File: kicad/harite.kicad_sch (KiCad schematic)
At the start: 76 parts, among them J1 Cirque Connector, J2 Cirque Connector, U1 RP2040_Zero, U2 RP2040_Zero

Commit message: basic schematic
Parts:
- removed D1, D10, D11, D12, D13, D14, D15, D16, D17, D18, D19, D2, D20, D21, D22, D23, D24, D25, D26, D27, D28, D29, D3, D30, D31, D32, D33, D34, D35, D36, D37, D38, D39, D4, D40, D41, D42, D43, D44, D45, D46, D47, D48, D49, D5, D50, D6, D7, D8, D9: D, ScottoKeebs_Components:Diode_SOD-123, symbol Device:D
- removed H1, H10, H2, H3, H4, H5, H6, H7, H8, H9: Mounting_Hole, MountingHole:MountingHole_2.2mm_M2_Pad_Via, symbol ScottoKeebs:Placeholder_Mounting_Hole
- removed J1, J2: Cirque Connector, footprints:Cirque-connector, symbol Connector_Generic:Conn_01x06
- removed S10, S6, S7, S8, S9: SKRHADE010, footprints:SKRHADE, symbol SKRHADE010:SKRHADE010
- removed U1, U2: RP2040_Zero, ScottoKeebs_MCU:RP2040_Zero, symbol ScottoKeebs:MCU_RP2040_Zero
- removed USB2: HRO-TYPE-C-31-M-12, footprints:HRO-TYPE-C-31-M-12, symbol USBType-C:HRO-TYPE-C-31-M-12
- added J1: 503480-0500, 5034800500, symbol 503480-0500:503480-0500
- added U3: Raspberry_Pi_Pico, ScottoKeebs_MCU:Raspberry_Pi_Pico, symbol ScottoKeebs:MCU_Raspberry_Pi_Pico
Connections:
- net Col 1 is gone; now on net GND: S1.5 (COMMON)
- net Col 2 is gone; now on net GND: S2.5 (COMMON)
- net Col 3 is gone; now on net GND: S3.5 (COMMON)
- net Col 4 is gone; now on net GND: S4.5 (COMMON)
- net Col 5 is gone; now on net GND: S5.5 (COMMON)
- net 3V3: now also J1.1, U3.36 (3V3)
- net 5V: now also U3.40 (VBUS)
- net GND: now also J1.4, U3.3 (GND)
- net GP0: now also U3.1 (GPIO0)
- net GP1: now also U3.2 (GPIO1)
- net TW: now reaches S5.3 (C)
- net TW: now also U3.25 (GPIO19)
- net PS: now reaches S1.6 (D)
- net PS: now also U3.7 (GPIO5)
- net PN: now reaches S1.1 (A)
- net PN: now also U3.4 (GPIO2)
- net PW: now reaches S1.3 (C)
- net PW: now also U3.5 (GPIO3)
- net PE: now reaches S1.4 (B)
- net PE: now also U3.6 (GPIO4)
- net IE: now reaches S4.4 (B)
- net IE: now also U3.21 (GPIO16)
- net TC: now reaches S5.2 (CENTER)
- net TC: now also U3.29 (GPIO22)
- net RN: now reaches S2.1 (A)
- net RN: now also U3.9 (GPIO6)
- net RW: now reaches S2.3 (C)
- net RW: now also U3.10 (GPIO7)
- net RE: now reaches S2.4 (B)
- net RE: now also U3.11 (GPIO8)
- net RS: now reaches S2.6 (D)
- net RS: now also U3.12 (GPIO9)
- net TN: now reaches S5.1 (A)
- net TN: now also U3.24 (GPIO18)
- net TE: now reaches S5.4 (B)
- net TE: now also U3.26 (GPIO20)
- net TS: now reaches S5.6 (D)
- net TS: now also U3.27 (GPIO21)
- net MW: now reaches S3.3 (C)
- net MW: now also U3.15 (GPIO11)
- net MS: now reaches S3.6 (D)
- net MS: now also U3.17 (GPIO13)
- net MN: now reaches S3.1 (A)
- net MN: now also U3.14 (GPIO10)
- net ME: now reaches S3.4 (B)
- net ME: now also U3.16 (GPIO12)
- net IN: now reaches S4.1 (A)
- net IN: now also U3.19 (GPIO14)
- net IW: now reaches S4.3 (C)
- net IW: now also U3.20 (GPIO15)
- net IS: now reaches S4.6 (D)
- net IS: now also U3.22 (GPIO17)
- new net JC: J1.3, U3.34 (GPIO28_ADC2)
- new net JX: J1.5, U3.31 (GPIO26_ADC0)
- new net JY: J1.2, U3.32 (GPIO27_ADC1)
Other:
- moved on the sheet: S5, USB1

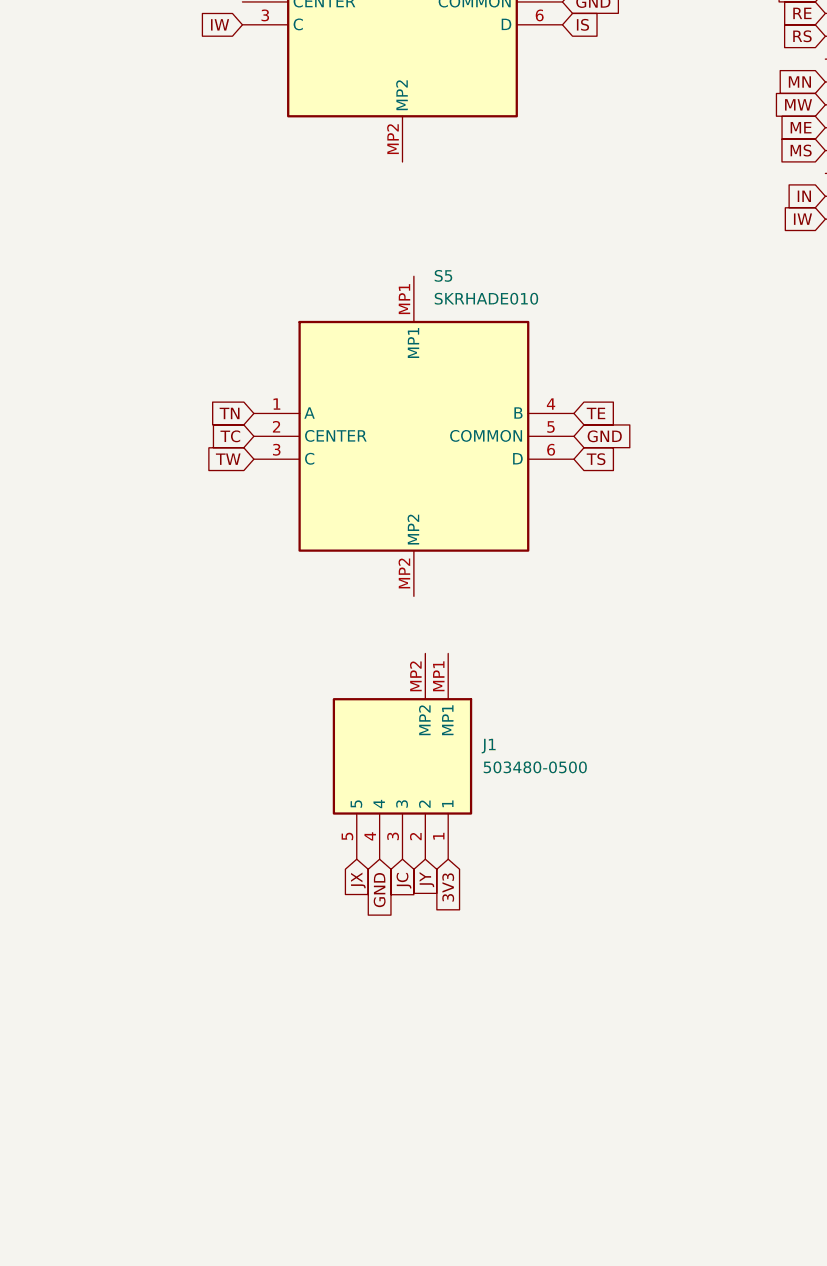
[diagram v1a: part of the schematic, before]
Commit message: Add 5034800540 and 5034801000
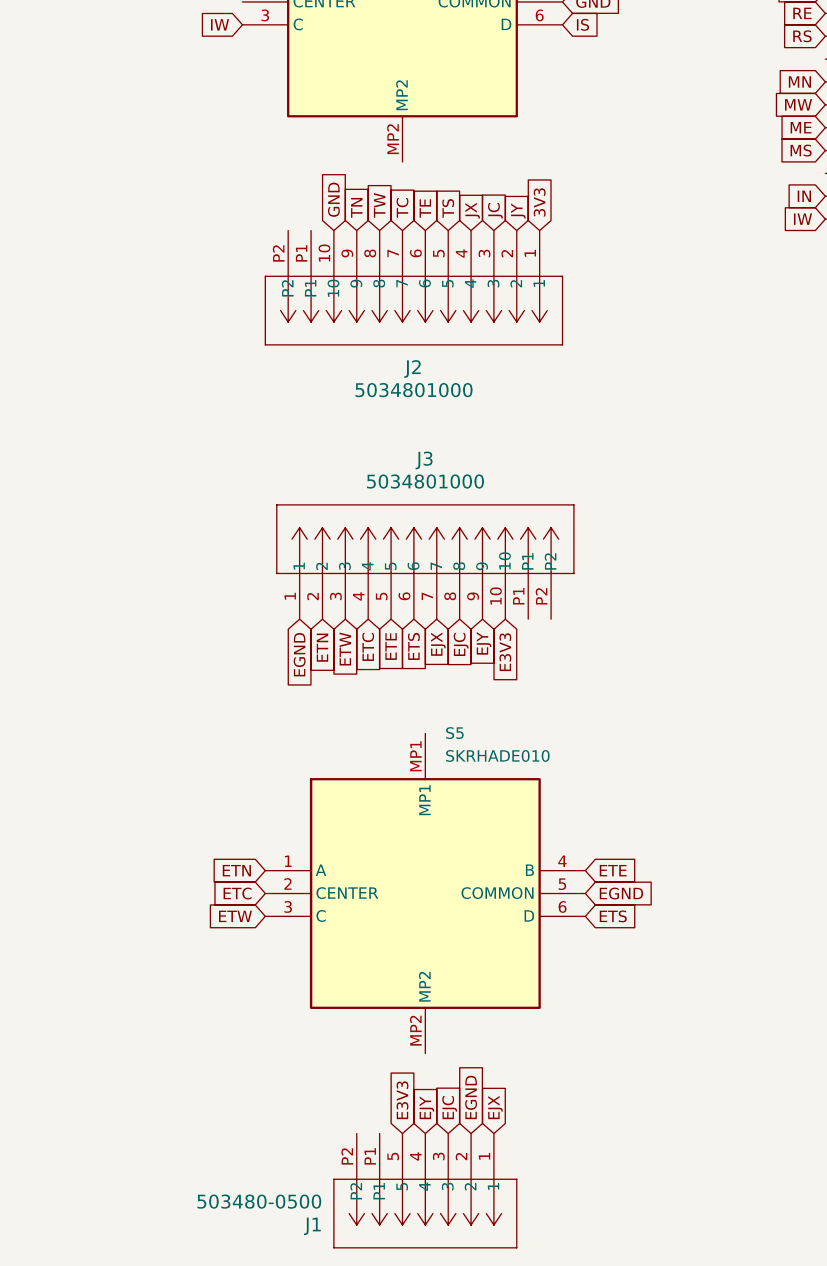
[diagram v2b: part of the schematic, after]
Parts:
- removed J1: 503480-0500, 5034800500, symbol 503480-0500:503480-0500
- added J1: 503480-0500, 5034800540, symbol 5034800540:5034800540
- added J2, J3: 5034801000, 5034801000, symbol 5034801000:5034801000
- S1, S2, S3, S4, S5: footprint footprints:SKRHADE -> SKRHADE010
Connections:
- net 3V3: now also J2.1
- net GND: now also J2.10; no longer S5.5 (COMMON)
- net JC: now also J2.3
- net JX: now also J2.4
- net JY: now also J2.2
- net TC: now also J2.7; no longer S5.2 (CENTER)
- net TE: now also J2.6; no longer S5.4 (B)
- net TN: now also J2.9; no longer S5.1 (A)
- net TS: now also J2.5; no longer S5.6 (D)
- net TW: now also J2.8; no longer S5.3 (C)
- new net E3V3: J1.5, J3.10
- new net EGND: J1.2, J3.1, S5.5 (COMMON)
- new net EJC: J1.3, J3.8
- new net EJX: J1.1, J3.7
- new net EJY: J1.4, J3.9
- new net ETC: J3.4, S5.2 (CENTER)
- new net ETE: J3.5, S5.4 (B)
- new net ETN: J3.2, S5.1 (A)
- new net ETS: J3.6, S5.6 (D)
- new net ETW: J3.3, S5.3 (C)
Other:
- moved on the sheet: S5

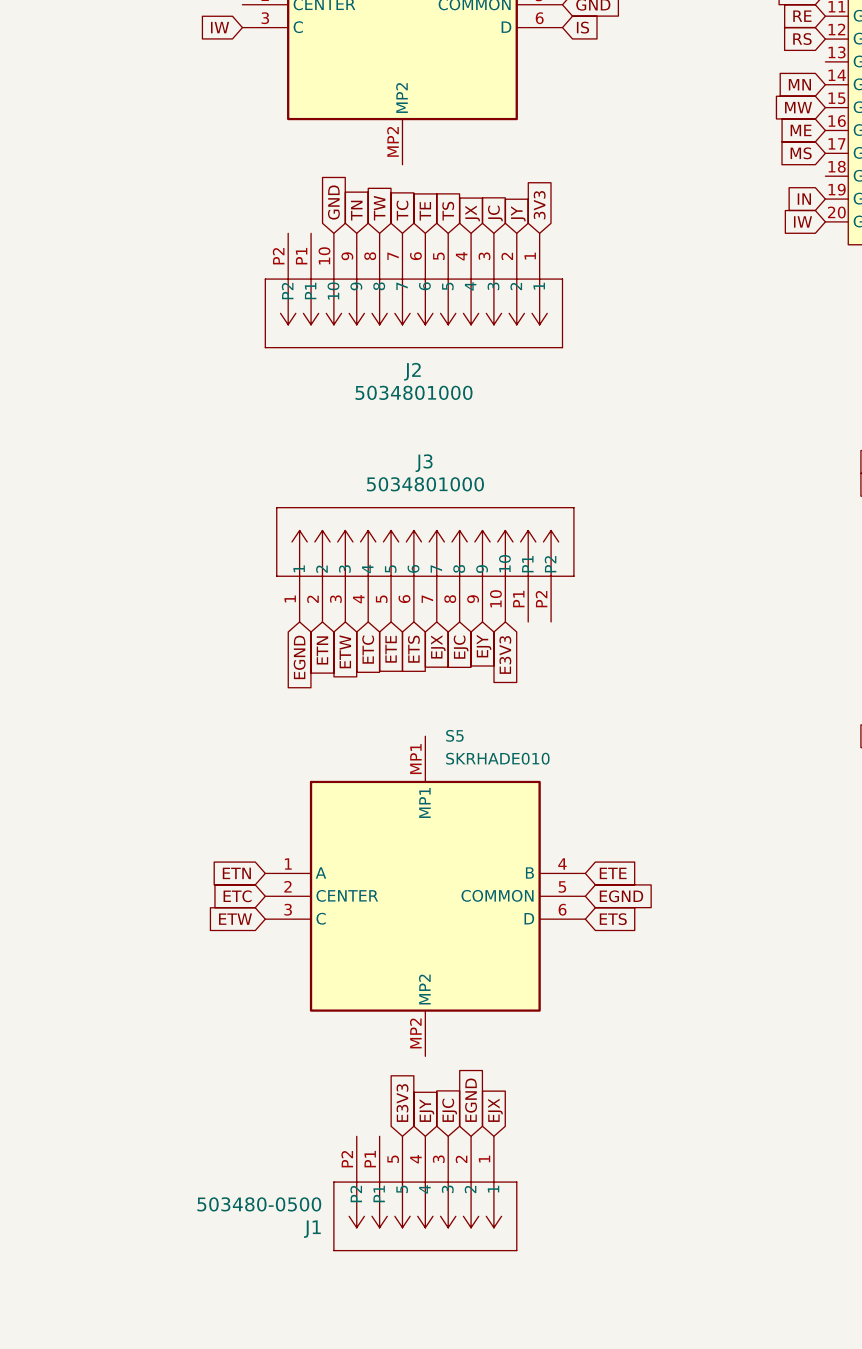
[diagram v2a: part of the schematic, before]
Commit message: fix orientation
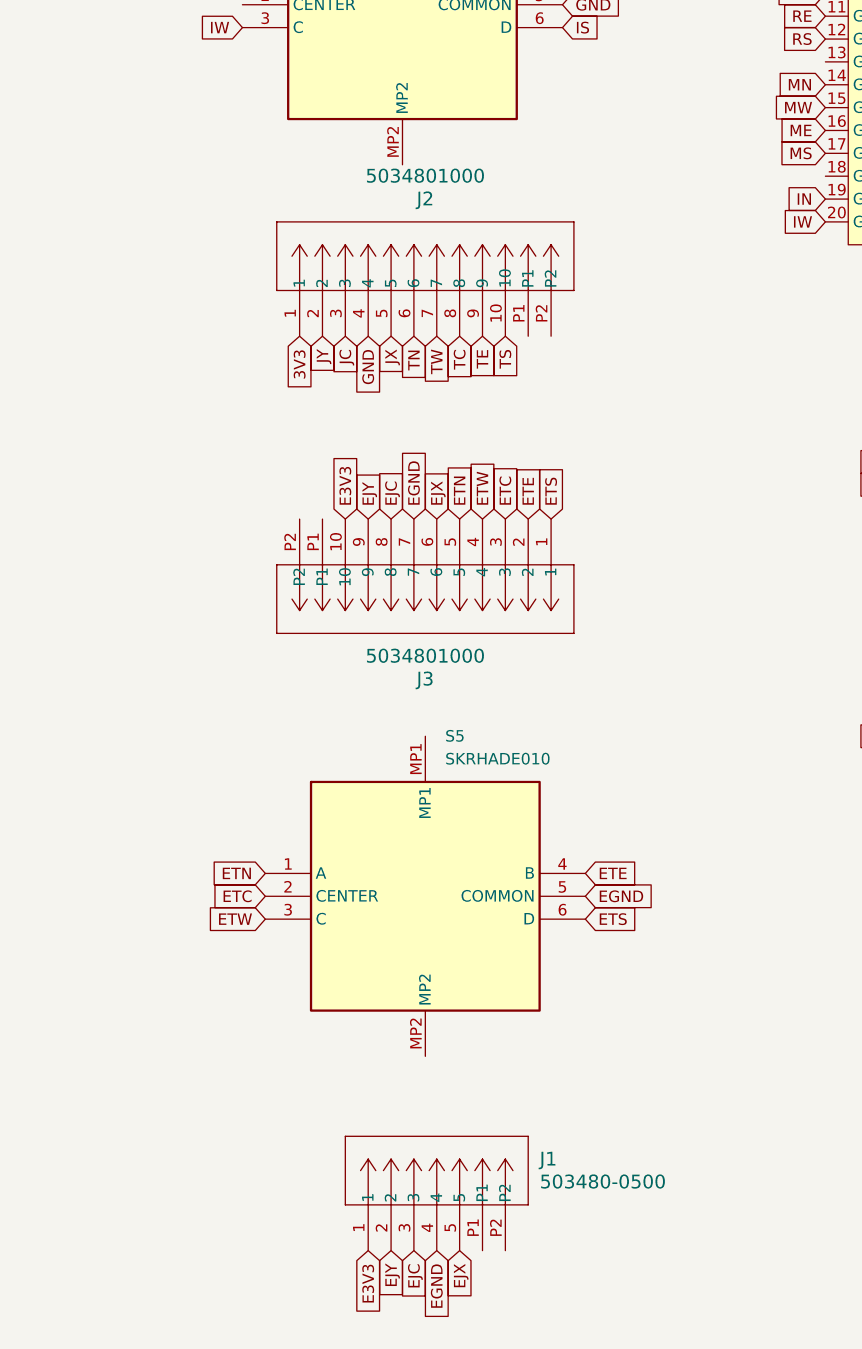
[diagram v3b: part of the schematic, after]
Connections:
- net E3V3: now also J1.1; no longer J1.5
- net EGND: now also J1.4, J3.7; no longer J1.2, J3.1
- net EJX: now also J1.5, J3.6; no longer J1.1, J3.7
- net EJY: now also J1.2; no longer J1.4
- net ETC: now also J3.3; no longer J3.4
- net ETE: now also J3.2; no longer J3.5
- net ETN: now also J3.5; no longer J3.2
- net ETS: now also J3.1; no longer J3.6
- net ETW: now also J3.4; no longer J3.3
- net GND: now also J2.4; no longer J2.10
- net JX: now also J2.5; no longer J2.4
- net TC: now also J2.8; no longer J2.7
- net TE: now also J2.9; no longer J2.6
- net TN: now also J2.6; no longer J2.9
- net TS: now also J2.10; no longer J2.5
- net TW: now also J2.7; no longer J2.8
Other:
- moved on the sheet: J1, J2, J3

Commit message: update
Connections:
- net RESET: now reaches S1.2 (CENTER)
- net RESET: now also U3.30 (RUN)
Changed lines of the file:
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@@
+		)
+	)
+	(global_label "RESET"
+		(shape input)
+		(at 332.74 59.69 0)
+		(fields_autoplaced yes)
+		(effects
+			(font
+				(size 1.27 1.27)
+			)
+			(justify left)
+		)
+		(property "Intersheetrefs" "${INTERSHEET_REFS}"
+			(at 341.4703 59.69 0)
+			(effects
+				(font
+					(size 1.27 1.27)
+				)
+				(justify left)
+				(hide yes)
+			)
 		)
 	)
@@
 			(effects
 				(font
+					(size 1.27 1.27)
+				)
+				(justify right)
+				(hide yes)
+			)
+		)
+	)
+	(global_label "RESET"
+		(shape input)
+		(at 27.94 58.42 180)
+		(fields_autoplaced yes)
+		(effects
+			(font
+				(size 1.27 1.27)
+			)
+			(justify right)
+		)
+		(property "Intersheetrefs" "${INTERSHEET_REFS}"
+			(at 19.2097 58.42 0)
+			(effects
+				(font
